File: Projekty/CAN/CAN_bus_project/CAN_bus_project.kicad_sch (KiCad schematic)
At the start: 38 parts, among them SW1 SW_DP3T, U1 MCP2515-xSO, U3 TJA1055T_3_C,518, U4 MCP2561-E-P, Y1 20MHz

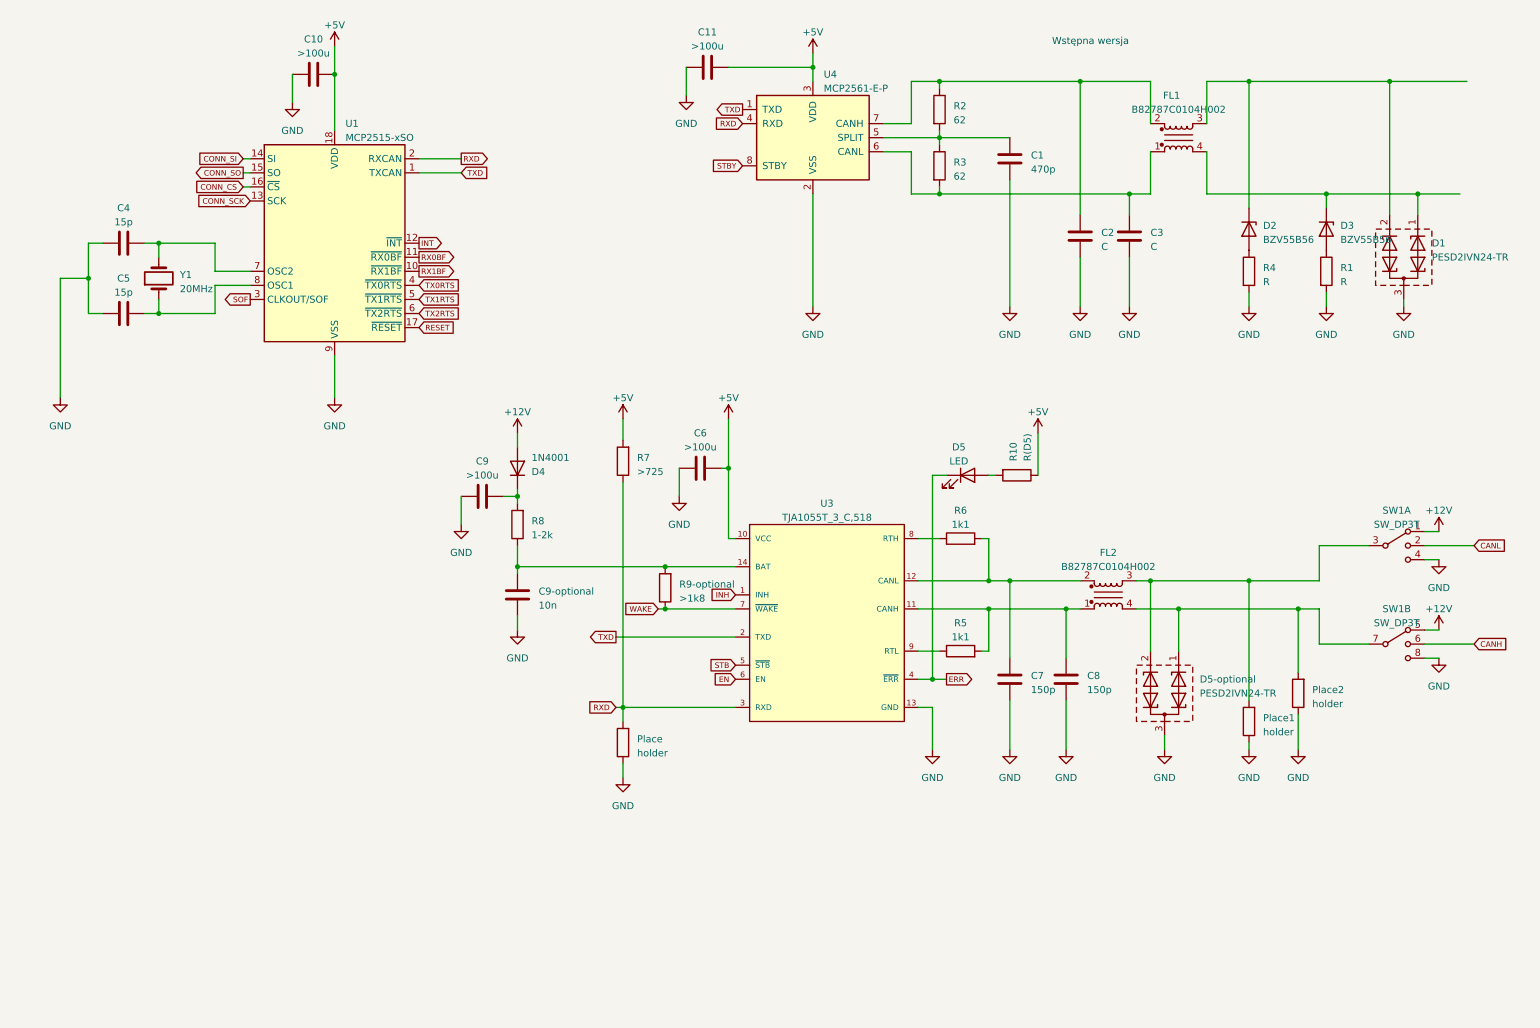
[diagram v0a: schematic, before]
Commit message: Schemat elektryczny CAN v0.2
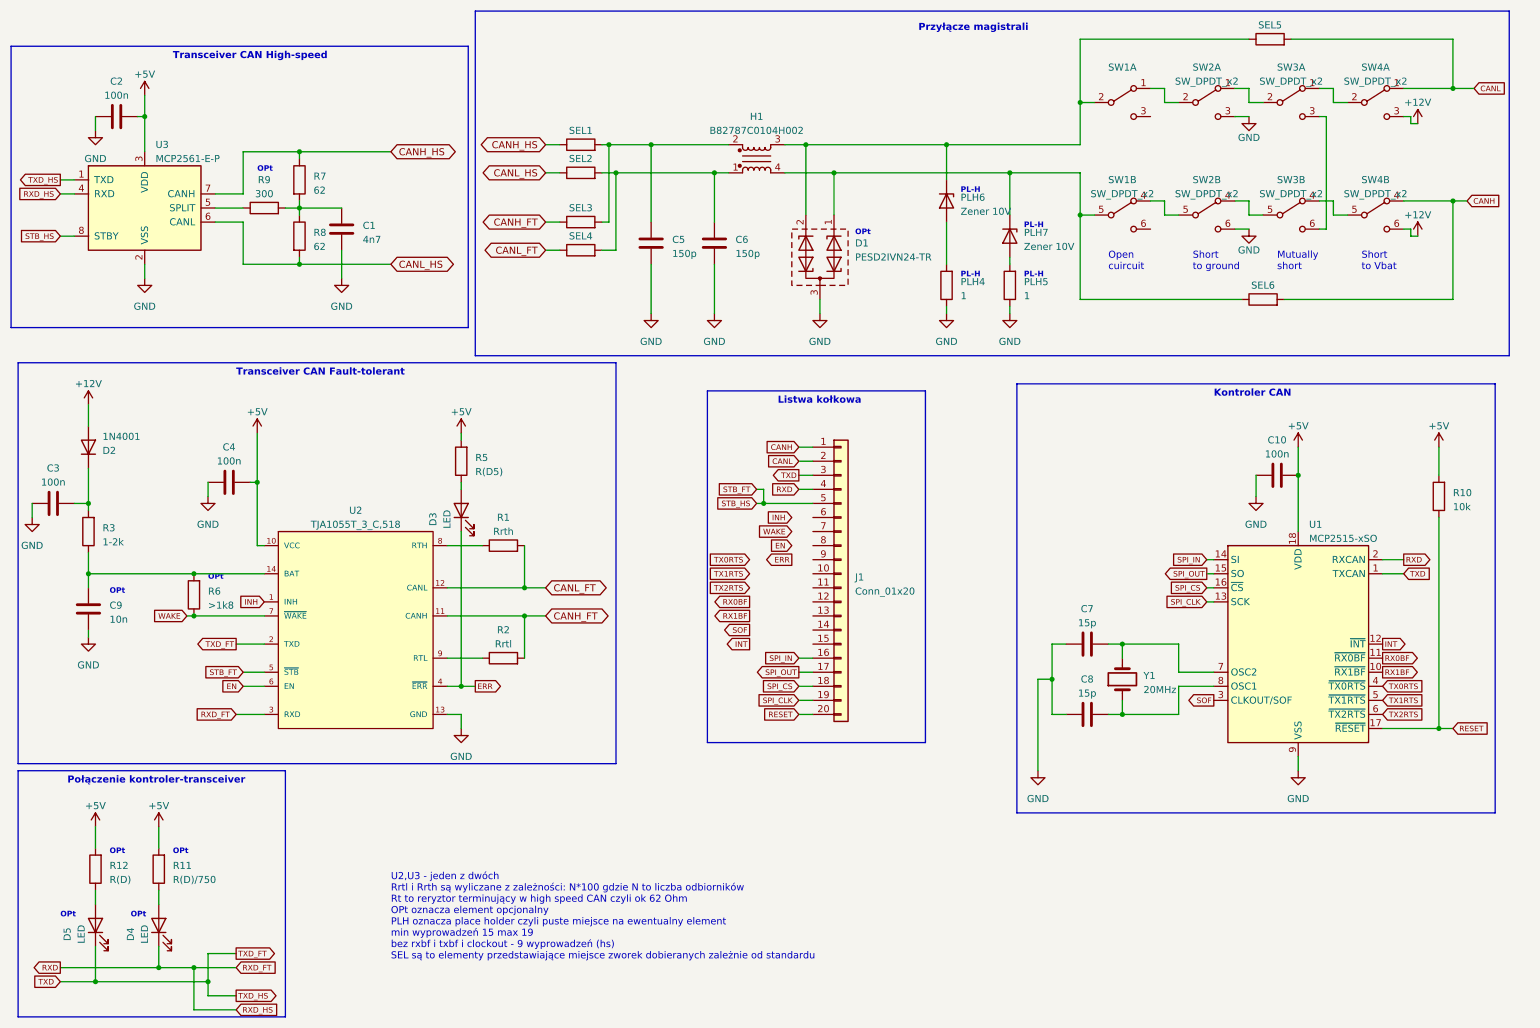
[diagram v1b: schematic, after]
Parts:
- removed C11: >100u, symbol Device:C
- removed C3: C, symbol Device:C
- removed D1: PESD2IVN24-TR, Package_TO_SOT_SMD:SOT-23, symbol Device:D_Zener_Dual_CommonCathode_AAK_Parallel
- removed D2, D3: BZV55B56, Diode_SMD:D_MiniMELF, symbol Diode:BZV55B56
- removed FL1: B82787C0104H002, symbol Device:Filter_EMI_LL_1423
- removed Place: holder, Resistor_THT:R_Axial_DIN0204_L3.6mm_D1.6mm_P7.62mm_Horizontal, symbol Device:R
- removed R1, R4: R, Resistor_THT:R_Axial_DIN0204_L3.6mm_D1.6mm_P7.62mm_Horizontal, symbol Device:R
- removed R7: >725, Resistor_THT:R_Axial_DIN0204_L3.6mm_D1.6mm_P7.62mm_Horizontal, symbol Device:R
- removed SW1: SW_DP3T, symbol Switch:SW_DP3T
- added D4, D5: LED, symbol Device:LED
- added J1: Conn_01x20, symbol Connector_Generic:Conn_01x20
- added PLH6, PLH7: Zener 10V, Diode_SMD:D_MiniMELF, symbol Diode:BZV55B56
- added R10: 10k, Resistor_THT:R_Axial_DIN0204_L3.6mm_D1.6mm_P7.62mm_Horizontal, symbol Device:R
- added R11: R(D)/750, Resistor_THT:R_Axial_DIN0204_L3.6mm_D1.6mm_P7.62mm_Horizontal, symbol Device:R
- added R12: R(D), Resistor_THT:R_Axial_DIN0204_L3.6mm_D1.6mm_P7.62mm_Horizontal, symbol Device:R
- added R9: 300, Resistor_THT:R_Axial_DIN0204_L3.6mm_D1.6mm_P7.62mm_Horizontal, symbol Device:R
- added SEL1, SEL2, SEL3, SEL4, SEL5, SEL6: ~, Resistor_THT:R_Axial_DIN0204_L3.6mm_D1.6mm_P7.62mm_Horizontal, symbol Device:R
- added SW1, SW2, SW3, SW4: SW_DPDT_x2, symbol Switch:SW_DPDT_x2
- C1: value 470p -> 4n7
- C10: value >100u -> 100n
- C2: value C -> 100n
- C3: renamed from C9; value >100u -> 100n
- C4: renamed from C6; value >100u -> 100n
- PLH4: renamed from Place1; value holder -> 1
- PLH5: renamed from Place2; value holder -> 1
- R1: renamed from R6; value 1k1 -> Rrth
- R2: renamed from R5; value 1k1 -> Rrtl
- renumbered C7 to C5, C8 to C6, C4 to C7, C5 to C8, C9-optional to C9, D5-optional to D1, D4 to D2, D5 to D3, FL2 to H1, R8 to R3, R10 to R5, R9-optional to R6, R2 to R7, R3 to R8, U3 to U2, U4 to U3
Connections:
- net STBY is gone; now on net STB_FT: U3.8 (STBY)
- net +12V: now also SW4.3 (C), SW4.6 (C)
- net +5V: now also C2.2, R5.2, R10.2, R11.2, R12.2; no longer R5.1
- net CANH: now also J1.1 (Pin_1), SEL6.2, SW4.4 (A)
- net CANL: now also J1.2 (Pin_2), SEL5.2, SW4.1 (A)
- net GND: now also C2.1, SW2.3 (C), SW2.6 (C); no longer C2.2
- net RESET: now also J1.20 (Pin_20), R10.1
- net RXD: now also D4.1 (K), J1.4 (Pin_4)
- net TXD: now also D5.1 (K), J1.3 (Pin_3)
- net at D1.1 (K), H1.4: now also PLH7.1 (K), SEL6.1, SW1.5 (B); no longer PLH5.2
- net at C1.1, R7.2, R8.1: now also R9.2; no longer U3.5 (SPLIT)
- net CANL_HS: now reaches R8.2, U3.6 (CANL)
- net CANL_HS: now also SEL2.1
- net CANH_HS: now reaches R7.1, U3.7 (CANH)
- net CANH_HS: now also SEL1.1; no longer C2.1
- net at C6.1, H1.1: now also SEL2.2, SEL4.2; no longer R2.2, U2.11 (CANH)
- net at C5.1, H1.2: now also SEL1.2, SEL3.2; no longer R1.2, U2.12 (CANL)
- net at D3.2 (A): now also R5.1; no longer R5.2
- net at D1.2 (K), H1.3: now also PLH6.1 (K), SEL5.1, SW1.2 (B); no longer PLH4.2
- net CONN_CS renamed SPI_CS
- net SPI_CS: now also J1.18 (Pin_18)
- net CONN_SCK renamed SPI_CLK
- net SPI_CLK: now also J1.19 (Pin_19)
- net CONN_SI renamed SPI_IN
- net SPI_IN: now also J1.16 (Pin_16)
- net CONN_SO renamed SPI_OUT
- net SPI_OUT: now also J1.17 (Pin_17)
- net STB renamed STB_FT
- net STB_FT: now also J1.5 (Pin_5)
- new net: PLH5.2, PLH7.2 (A)
- new net: R9.1, U3.5 (SPLIT)
- new net: SW1.4 (A), SW2.5 (B)
- new net: D5.2 (A), R12.1
- new net: SW2.1 (A), SW3.2 (B)
- new net: SW1.1 (A), SW2.2 (B)
- new net: D4.2 (A), R11.1
- new net: PLH4.2, PLH6.2 (A)
- new net: SW2.4 (A), SW3.5 (B)
- new net: SW3.4 (A), SW4.5 (B)
- new net: SW3.1 (A), SW4.2 (B)
- new net: SW3.3 (C), SW3.6 (C)
- new net CANH_FT: R2.2, SEL3.1, U2.11 (CANH)
- new net CANL_FT: R1.2, SEL4.1, U2.12 (CANL)
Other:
- note added: "Kontroler CAN"
- note added: "Listwa kołkowa"
- note added: "Mutually short"
- note added: "OPt"
- note added: "Open cuircuit"
- note added: "PL-H"
- note added: "Połączenie kontroler-transceiver"
- note added: "Przyłącze magistrali"
- note added: "Short to Vbat"
- note added: "Short to ground"
- note added: "Transceiver CAN Fault-tolerant"
- note added: "Transceiver CAN High-speed"
- note added: "U2,U3 - jeden z dwóch Rrtl i Rrth są wyliczane z zależności: N*100 gdzie N to liczba odbiorników Rt to reryztor terminujący w high speed CAN czyli ok 62 Ohm OPt oznacza element opcjonalny PLH oznacza place holder czyli puste miejsce na ewentualny element min wyprowadzeń 15 max 19 bez rxbf i txbf i clockout - 9 wyprowadzeń (hs) SEL są to elementy przedstawiające miejsce zworek dobieranych zależnie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"
- note removed: "Wstępna wersja"
- company: (none) -> PŁ
- title: (none) -> Przyłącze do sieci CAN (high-speed i fault-toletant)
- moved on the sheet: C1, C10, C3, C4, C5, C6, C7, C8, C9, D1, D2, D3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

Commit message: Schemat elektryczny CAN v0.3
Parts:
- removed SW1, SW2, SW3, SW4: SW_DPDT_x2, symbol Switch:SW_DPDT_x2
- added J2: Screw_Terminal_01x02, Connector_Samtec_HPM_THT:Samtec_HPM-02-05-x-S_Straight_1x02_Pitch5.08mm, symbol Connector:Screw_Terminal_01x02
- added J3, J4: Conn_01x02, symbol Connector_Generic:Conn_01x02
- added SW1, SW2, SW3, SW4, SW5, SW6, SW7, SW8: SW_SPDT, 1_WLASNA_Library:3PAD_WIRE_SWITCH, symbol Switch:SW_SPDT
- C1, C5, C6: footprint (none) -> Capacitor_THT:C_Disc_D5.0mm_W2.5mm_P5.00mm
- C10, C2, C3, C4: footprint (none) -> Capacitor_THT:C_Disc_D5.0mm_W2.5mm_P2.50mm
- C7, C8: footprint (none) -> Capacitor_THT:C_Disc_D7.0mm_W2.5mm_P5.00mm
- C9: footprint (none) -> Capacitor_THT:C_Disc_D11.0mm_W5.0mm_P7.50mm
- D3, D4, D5: footprint (none) -> 1_WLASNA_Library:2PAD_WIRE
- D6: renamed from PLH6; footprint Diode_SMD:D_MiniMELF -> Diode_THT:D_DO-35_SOD27_P10.16mm_Horizontal
- D7: renamed from PLH7; footprint Diode_SMD:D_MiniMELF -> Diode_THT:D_DO-35_SOD27_P10.16mm_Horizontal
- H1: footprint (none) -> 1_WLASNA_Library:4Pin_COMMON_MODE_CHOKE_B82787C0104H002
- J1: footprint (none) -> Connector_PinSocket_2.54mm:PinSocket_2x20_P2.54mm_Vertical
- R1, R2, R3: footprint Resistor_THT:R_Axial_DIN0204_L3.6mm_D1.6mm_P7.62mm_Horizontal -> Resistor_THT:R_Axial_DIN0207_L6.3mm_D2.5mm_P10.16mm_Horizontal
- R10: renamed from R11; footprint Resistor_THT:R_Axial_DIN0204_L3.6mm_D1.6mm_P7.62mm_Horizontal -> Resistor_THT:R_Axial_DIN0207_L6.3mm_D2.5mm_P10.16mm_Horizontal
- R11: renamed from R12; footprint Resistor_THT:R_Axial_DIN0204_L3.6mm_D1.6mm_P7.62mm_Horizontal -> Resistor_THT:R_Axial_DIN0207_L6.3mm_D2.5mm_P10.16mm_Horizontal
- R12: renamed from PLH4; footprint Resistor_THT:R_Axial_DIN0204_L3.6mm_D1.6mm_P7.62mm_Horizontal -> Resistor_THT:R_Axial_DIN0207_L6.3mm_D2.5mm_P10.16mm_Horizontal
- R13: renamed from PLH5; footprint Resistor_THT:R_Axial_DIN0204_L3.6mm_D1.6mm_P7.62mm_Horizontal -> Resistor_THT:R_Axial_DIN0207_L6.3mm_D2.5mm_P10.16mm_Horizontal
- R4: renamed from R5; value R(D5) -> R(D3); footprint Resistor_THT:R_Axial_DIN0204_L3.6mm_D1.6mm_P7.62mm_Horizontal -> Resistor_THT:R_Axial_DIN0207_L6.3mm_D2.5mm_P10.16mm_Horizontal
- R5: renamed from R6; footprint Resistor_THT:R_Axial_DIN0204_L3.6mm_D1.6mm_P7.62mm_Horizontal -> Resistor_THT:R_Axial_DIN0207_L6.3mm_D2.5mm_P10.16mm_Horizontal
- R6: renamed from R7; footprint Resistor_THT:R_Axial_DIN0204_L3.6mm_D1.6mm_P7.62mm_Horizontal -> Resistor_THT:R_Axial_DIN0207_L6.3mm_D2.5mm_P10.16mm_Horizontal
- R7: renamed from R8; footprint Resistor_THT:R_Axial_DIN0204_L3.6mm_D1.6mm_P7.62mm_Horizontal -> Resistor_THT:R_Axial_DIN0207_L6.3mm_D2.5mm_P10.16mm_Horizontal
- R8: renamed from R9; footprint Resistor_THT:R_Axial_DIN0204_L3.6mm_D1.6mm_P7.62mm_Horizontal -> Resistor_THT:R_Axial_DIN0207_L6.3mm_D2.5mm_P10.16mm_Horizontal
- R9: renamed from R10; footprint Resistor_THT:R_Axial_DIN0204_L3.6mm_D1.6mm_P7.62mm_Horizontal -> Resistor_THT:R_Axial_DIN0207_L6.3mm_D2.5mm_P10.16mm_Horizontal
- SEL1, SEL2, SEL3, SEL4, SEL5, SEL6: footprint Resistor_THT:R_Axial_DIN0204_L3.6mm_D1.6mm_P7.62mm_Horizontal -> Resistor_SMD:R_0805_2012Metric
- Y1: footprint (none) -> Crystal:Crystal_SMD_HC49-SD_HandSoldering
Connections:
- net +12V: now also J4.1 (Pin_1), SW4.3 (C), SW8.3 (C)
- net +5V: now also J3.1 (Pin_1)
- net CANH: now also J2.1 (Pin_1), SW8.1 (A)
- net CANL: now also J2.2 (Pin_2), SW4.1 (A)
- net EN: now also J1.7 (Pin_7)
- net ERR: now also J1.8 (Pin_8)
- net GND: now also J3.2 (Pin_2), J4.2 (Pin_2), SW2.3 (C), SW6.3 (C)
- net INT: now also J1.15 (Pin_15)
- net RX0BF: now also J1.12 (Pin_12)
- net RX1BF: now also J1.13 (Pin_13)
- net SOF: now also J1.14 (Pin_14)
- net TX0RTS: now also J1.9 (Pin_9)
- net TX1RTS: now also J1.10 (Pin_10)
- net TX2RTS: now also J1.11 (Pin_11)
- net WAKE: now also J1.6 (Pin_6)
- net at D1.1 (K), D7.1 (K), H1.4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: now also SW5.2 (B)
- net at D1.2 (K), D6.1 (K), H1.3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: now also SW1.2 (B)
- net INH: no longer names the net of U2.1 (INH)
- new net: SW3.1 (A), SW4.2 (B)
- new net: SW2.1 (A), SW3.2 (B)
- new net: SW3.3 (C), SW7.3 (C)
- new net: SW1.1 (A), SW2.2 (B)
- new net: SW7.1 (A), SW8.2 (B)
- new net: SW6.1 (A), SW7.2 (B)
- new net: SW5.1 (A), SW6.2 (B)
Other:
- note removed: "PL-H"
- moved on the sheet: J1
